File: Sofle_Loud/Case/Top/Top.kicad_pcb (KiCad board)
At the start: 2 copper layers, 143.5 x 114.2 mm, 43 parts, among them Q2 TIP120, SW1 SW_PUSH_LED, SW10 SW_PUSH_LED, SW11 SW_PUSH_LED, SW12 SW_PUSH_LED, SW13 SW_PUSH_LED, SW14 SW_PUSH_LED, SW15 SW_PUSH_LED, SW16 SW_PUSH_LED, SW17 SW_PUSH_LED, SW18 SW_PUSH_LED, SW19 SW_PUSH_LED, SW2 SW_PUSH_LED, SW20 SW_PUSH_LED, SW21 SW_PUSH_LED, SW22 SW_PUSH_LED, SW23 SW_PUSH_LED, SW24 SW_PUSH_LED, SW25 Rotary_Encoder_Switch, SW26 SW_PUSH_LED, SW27 SW_PUSH_LED, SW28 SW_PUSH_LED, SW29 SW_PUSH_LED, SW3 SW_PUSH_LED, SW30 SW_PUSH_LED, SW4 SW_PUSH_LED, SW5 SW_PUSH_LED, SW6 SW_PUSH_LED, SW7 SW_PUSH_LED, SW8 SW_PUSH_LED, SW9 SW_PUSH_LED, U2 Solenoid

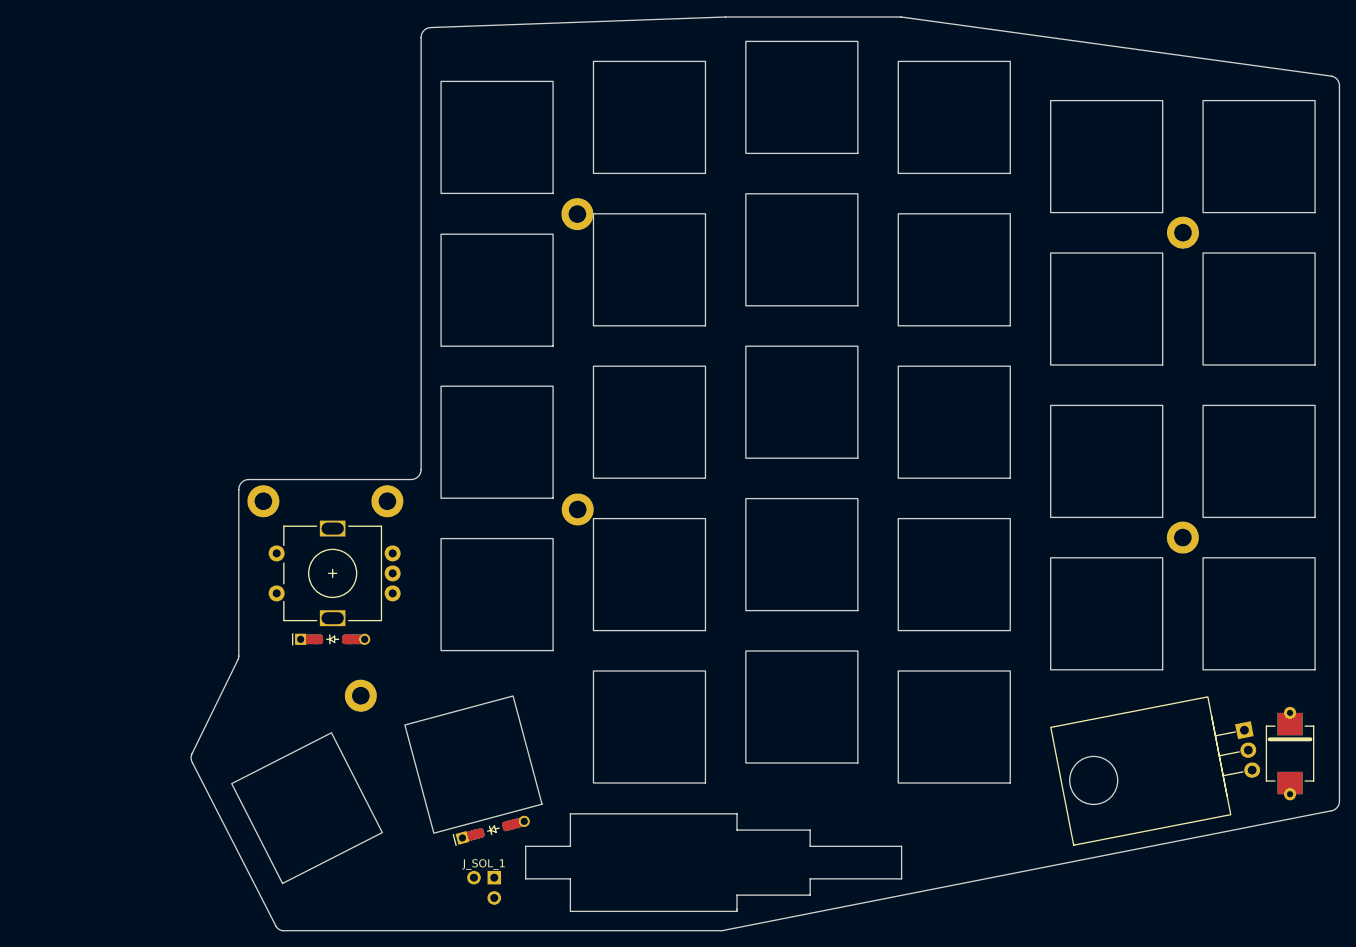
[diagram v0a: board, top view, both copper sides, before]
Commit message: SENT THIS VERSION OUT FOR PRODUCTION created key plates created top plates above key plates tweaked component layout to make room for plate M2 f-f spacers
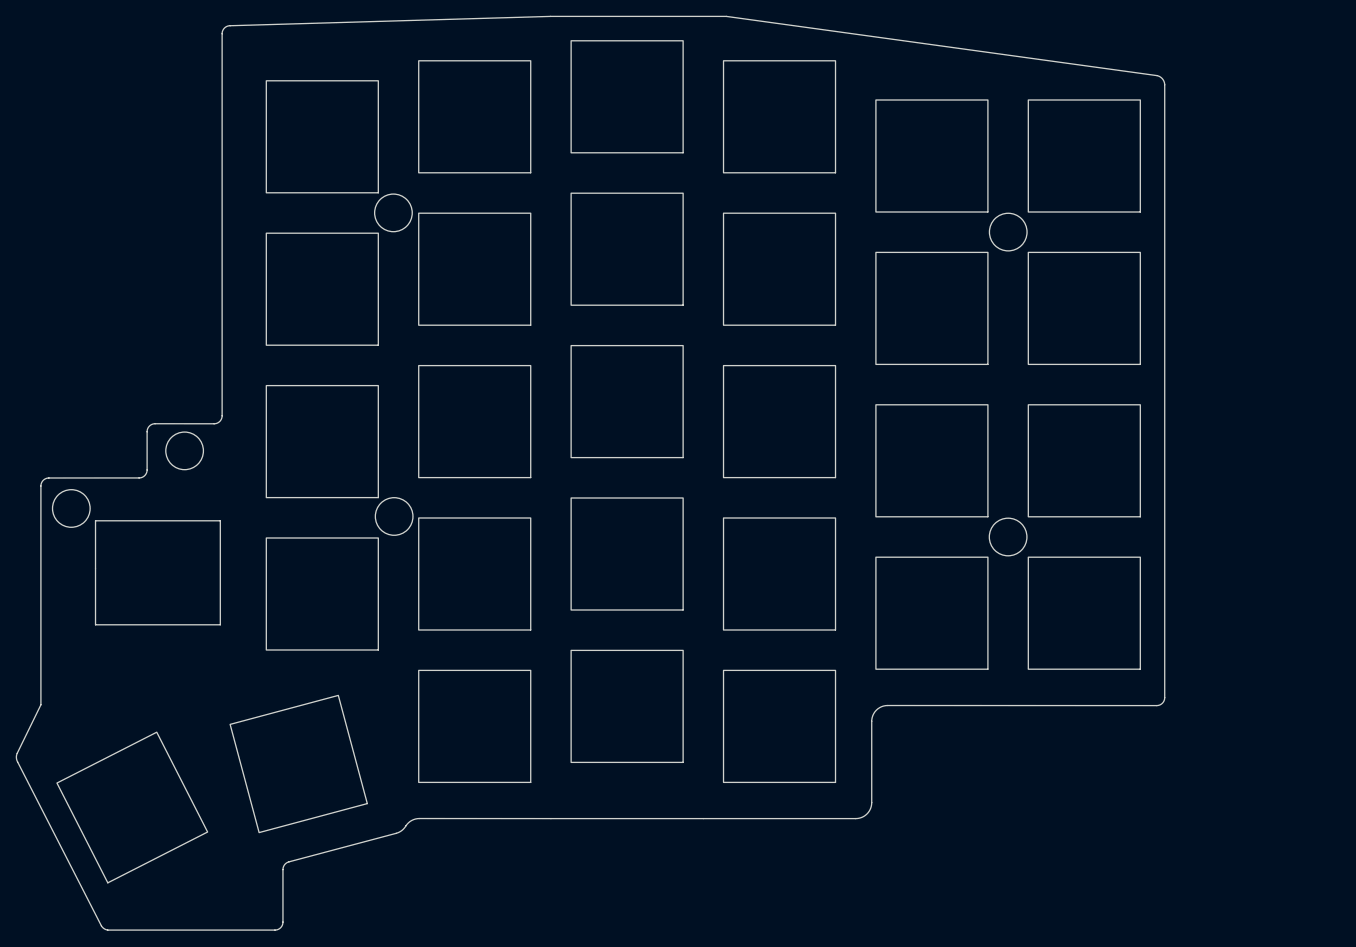
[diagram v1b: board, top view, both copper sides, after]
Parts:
- removed D25, D27: D, SofleChocLoud:D_SOD-123_DO-35_Hybrid_DoubleSided
- removed D_SOL_1: MUR340S, SofleChocLoud:MUR340S_IN4001_TH_HYBRID
- removed J_SOL_1: Conn_01x02_Female, SofleChocLoud:PinHeader_1x02_P2.54mm_L-Shaped
- removed Q2: TIP120, SofleChocLoud:TO-220-3_Horizontal_TabUp
- removed TH7: HOLE, SofleChocLoud:M2_HOLE_PCB
- removed U2: Solenoid, SofleLoud:uxcell a14092600ux0438 solenoid cutout
- SW25: footprint SofleChocLoud:RotaryEncoder_Alps_EC11E-Switch_Vertical_H20mm-keebio_modified -> SofleLoud:RotaryEncoder_hole
- TH1, TH2, TH3, TH4, TH5, TH6: footprint SofleChocLoud:M2_HOLE_PCB -> SofleChocLoud:M2_HOLE_PCB_through_hole
- moved TH2 26.1 mm to (77.7, 95.6)
- moved TH1 24.0 mm to (63.6, 102.8)
- moved TH3 23.0 mm to (103.8, 65.9)
- moved TH5 23.0 mm to (103.9, 103.8)
- moved SW7 21.8 mm to (95.0, 75.4)
- moved SW11 21.8 mm to (171.2, 77.8)
- moved SW15 21.8 mm to (133.1, 89.5)
- moved SW17 21.8 mm to (171.2, 96.9)
- moved SW21 21.8 mm to (133.1, 108.5)
- moved SW23 21.8 mm to (171.2, 115.9)
- moved SW29 21.8 mm to (133.1, 127.6)
- moved SW3 21.8 mm to (133.1, 51.4)
- moved SW5 21.8 mm to (171.2, 58.8)
- moved SW9 21.8 mm to (133.1, 70.4)
- moved TH6 21.8 mm to (180.7, 106.4)
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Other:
- outline, holes or cut-outs redrawn
- board text added: "JLCJLCJLCJLC"
- board text added: "s1"
- board text added: "s10"
- board text added: "s11"
- board text added: "s12"
- board text added: "s13"
- board text added: "s14"
- board text added: "s15"
- board text added: "s16"
- board text added: "s17"
- board text added: "s18"
- board text added: "s19"
- board text added: "s2"
- board text added: "s20"
- board text added: "s21"
- board text added: "s22"
- board text added: "s23"
- board text added: "s24"
- board text added: "s26"
- board text added: "s27"
- board text added: "s28"
- board text added: "s29"
- board text added: "s3"
- board text added: "s30"
- board text added: "s4"
- board text added: "s5"
- board text added: "s6"
- board text added: "s7"
- board text added: "s8"
- board text added: "s9"
